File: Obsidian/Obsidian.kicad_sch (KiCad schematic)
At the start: 5 parts

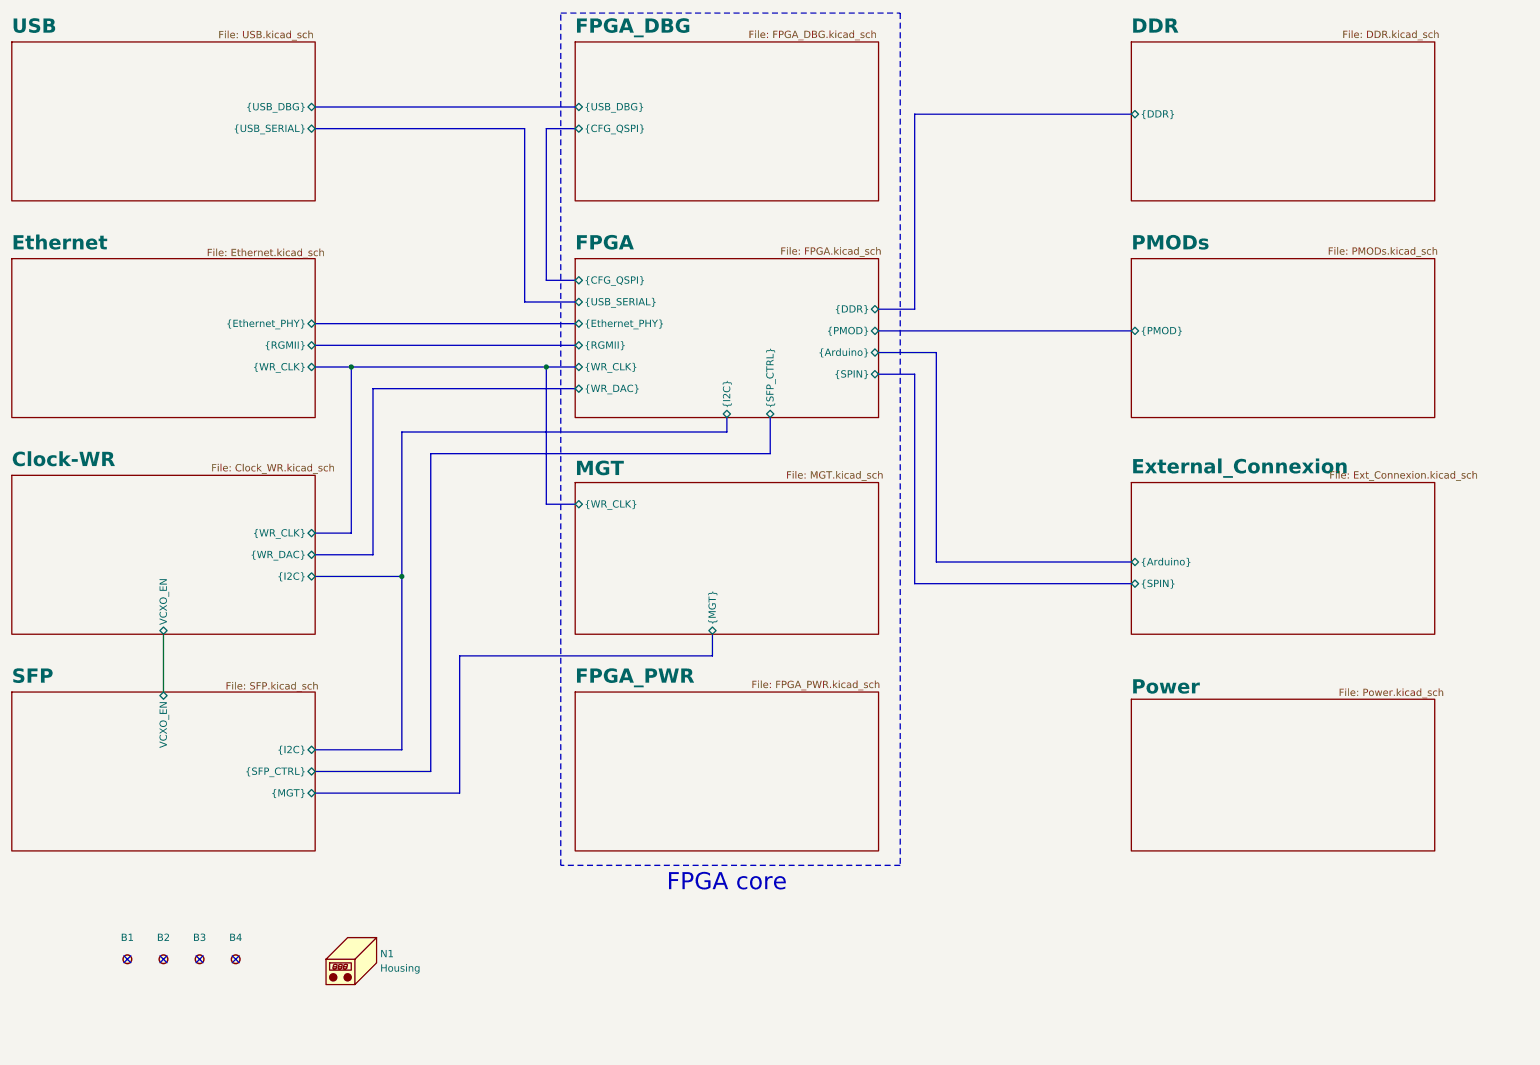
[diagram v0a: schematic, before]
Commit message: removing reset global label
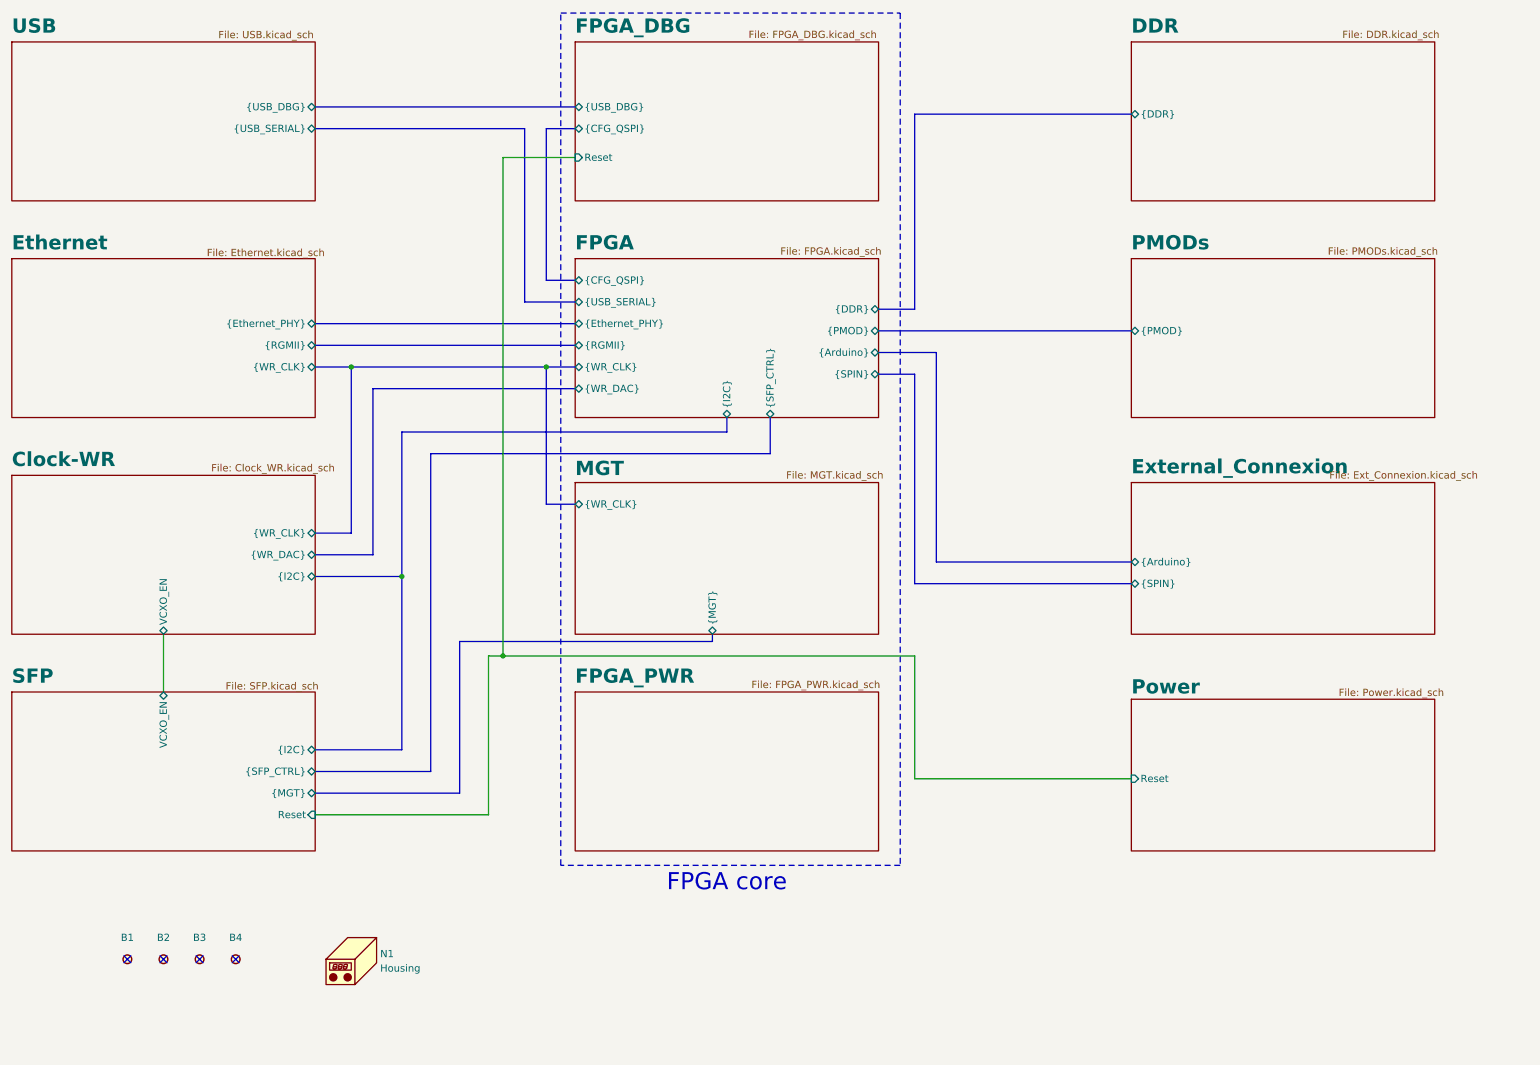
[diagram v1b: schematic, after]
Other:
- sheet FPGA_DBG ports: added Reset; removed none
- sheet Power ports: added Reset; removed none
- sheet SFP ports: added Reset; removed none
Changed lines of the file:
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@@
 	)
 	(junction
+		(at 106.68 127)
+		(diameter 0)
+		(color 0 0 0 0)
+	)
+	(junction
 		(at 88.9 113.03)
 		(diameter 0)
@@
 		)
 	)
+	(wire
+		(pts
+			(xy 104.14 127) (xy 104.14 154.94)
+		)
+		(stroke
+			(width 0)
+			(type default)
+		)
+	)
 	(bus
 		(pts
-			(xy 143.51 127) (xy 99.06 127)
+			(xy 143.51 124.46) (xy 99.06 124.46)
 		)
 		(stroke
@@
 	(bus
 		(pts
-			(xy 99.06 127) (xy 99.06 151.13)
+			(xy 99.06 124.46) (xy 99.06 151.13)
 		)
 		(stroke
@@
 	(bus
 		(pts
-			(xy 143.51 123.19) (xy 143.51 127)
+			(xy 143.51 123.19) (xy 143.51 124.46)
+		)
+		(stroke
+			(width 0)
+			(type default)
+		)
+	)
+	(wire
+		(pts
+			(xy 217.17 148.59) (xy 179.07 148.59)
+		)
+		(stroke
+			(width 0)
+			(type default)
+		)
+	)
+	(wire
+		(pts
+			(xy 179.07 127) (xy 106.68 127)
 		)
 		(stroke
@@
 		)
 	)
+	(wire
+		(pts
+			(xy 104.14 127) (xy 106.68 127)
+		)
+		(stroke
+			(width 0)
+			(type default)
+		)
+	)
+	(wire
+		(pts
+			(xy 119.38 39.37) (xy 106.68 39.37)
+		)
+		(stroke
+			(width 0)
+			(type default)
+		)
+	)
 	(bus
 		(pts
@@
 		)
 	)
+	(wire
+		(pts
+			(xy 179.07 148.59) (xy 179.07 127)
+		)
+		(stroke
+			(width 0)
+			(type default)
+		)
+	)
 	(bus
 		(pts
@@
 		)
 	)
+	(wire
+		(pts
+			(xy 104.14 154.94) (xy 73.66 154.94)
+		)
+		(stroke
+			(width 0)
+			(type default)
+		)
+	)
 	(bus
 		(pts
@@
 		)
 	)
+	(wire
+		(pts
+			(xy 106.68 39.37) (xy 106.68 127)
+		)
+		(stroke
+			(width 0)
+			(type default)
+		)
+	)
 	(bus
 		(pts
@@
 			)
 		)
+		(pin "Reset" input
+			(at 217.17 148.59 180)
+			(effects
+				(font
+					(size 1.27 1.27)
+				)
+				(justify left)
+			)
+		)
 		(instances
 			(project "Obsidian"
@@
 			)
 		)
+		(pin "Reset" input
+			(at 119.38 39.37 180)
+			(effects
+				(font
+					(size 1.27 1.27)
+				)
+				(justify left)
+			)
+		)
 		(instances
 			(project "Obsidian"
@@
 			(effects
 				(font
+					(size 1.27 1.27)
+				)
+				(justify right)
+			)
+		)
+		(pin "Reset" input
+			(at 73.66 154.94 0)
+			(effects
+				(font

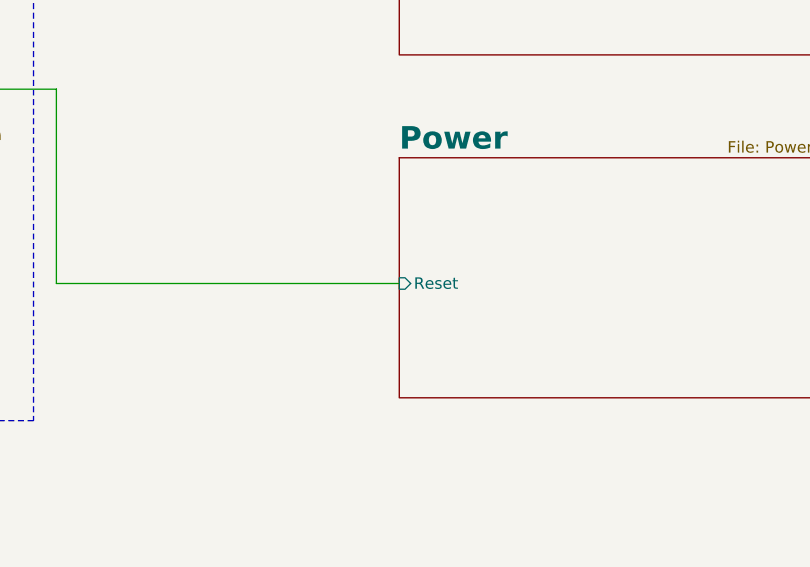
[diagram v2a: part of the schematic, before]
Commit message: Adding documentation for configuration with flash memory, adding more comments to schematic
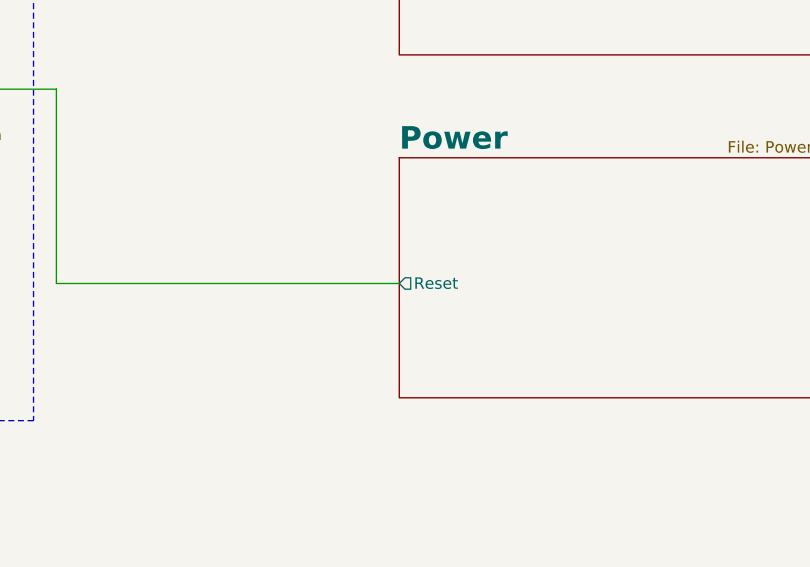
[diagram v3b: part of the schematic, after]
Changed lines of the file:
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@@
 			)
 		)
-		(pin "Reset" input
+		(pin "Reset" output
 			(at 217.17 148.59 180)
 			(effects

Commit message: Cleaning symbol fields
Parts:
- B1, B2, B3, B4: Author CERN DEM JMW -> (none); Case (none) -> (none); Comment (none) -> (none); Component Kind Standard (No BOM) -> (none); Component Type Standard (No BOM) -> (none); ComponentHeight 0mm -> (none); ComponentLink1Description (none) -> (none); ComponentLink1URL (none) -> (none); ComponentLink2Description (none) -> (none); ComponentLink2URL (none) -> (none); CreateDate 10/01/12 00:00:00 -> (none); Database Table Name Eletro-mechanical -> (none); Family Plated Hole -> (none); Footprint Library Pads -> (none); Footprint Path PcbLib\Pads.PcbLib -> (none); Footprint Ref MTG320_550 -> (none); HelpURL Undefined -> (none); LatestRevisionDate 10/01/12 00:00:00 -> (none); Library Name Pads -> (none); Library Path SchLib\Pads.SchLib -> (none); Library Ref Single Terminal Socket -> (none); License CC-BY-SA 4.0 -> (none); Manufacturer (none) -> (none); Manufacturer Part Number (none) -> (none); Manufacturer1 ComponentHeight (none) -> (none); Manufacturer1 Example (none) -> (none); Manufacturer1 Part Number (none) -> (none); Mounted No -> (none); PackageDescription Plated Through Hole: Hole Dia.=3.2mm Pad Dia.=5.5mm -> (none); Part Description Plated Through Hole: Hole Dia.=3.2mm Pad Dia.=5.5mm -> (none); Part Number PLATED_HOLE3.2_PAD5.5 -> (none); Pin Count 1 -> (none); SCEM (none) -> (none); SMD No -> (none); Sense No -> (none); Sense Comment (none) -> (none); Socket No -> (none); Status None -> (none); Status Comment (none) -> (none)

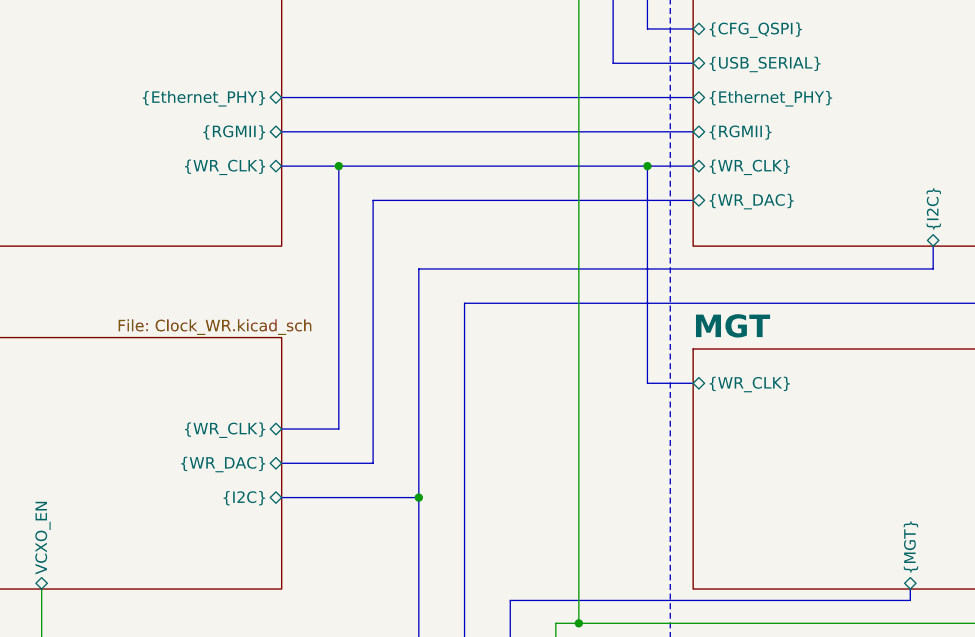
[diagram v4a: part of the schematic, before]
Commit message: Separating auxiliary clock from WR clock
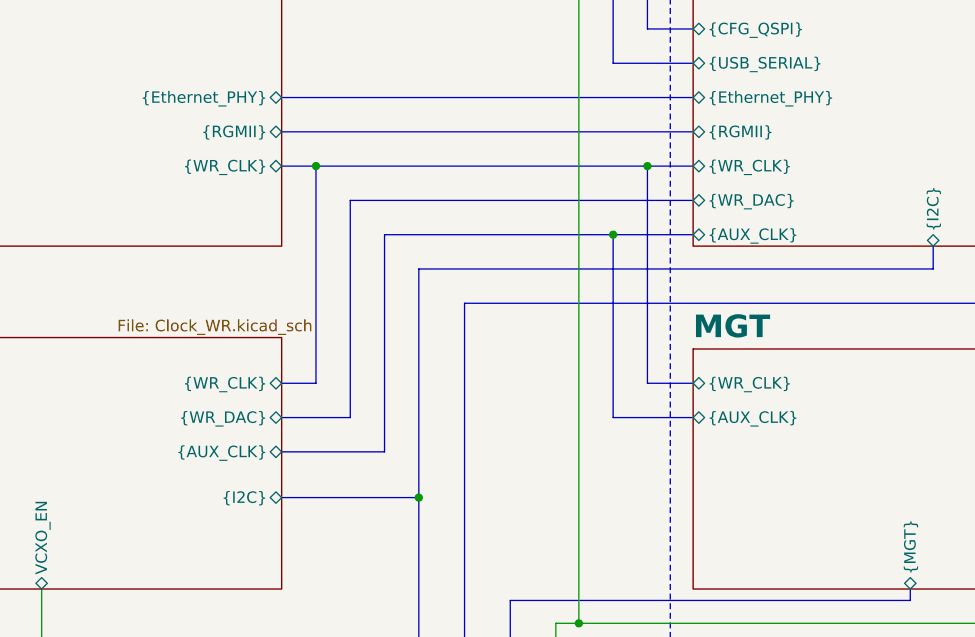
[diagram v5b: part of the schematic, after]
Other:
- sheet Clock-WR ports: added {AUX_CLK}; removed none
- sheet FPGA ports: added {AUX_CLK}; removed none
- sheet MGT ports: added {AUX_CLK}; removed none
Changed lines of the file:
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@@
+	)
+	(junction
+		(at 77.47 76.2)
+		(diameter 0)
+		(color 0 0 0 0)
+	)
+	(junction
+		(at 110.49 83.82)
+		(diameter 0)
+		(color 0 0 0 0)
 	)
 	(junction
@@
 		(color 0 0 0 0)
 	)
-	(junction
-		(at 80.01 76.2)
-		(diameter 0)
-		(color 0 0 0 0)
-	)
 	(no_connect
 		(at 40.64 180.34)
@@
 	(bus
 		(pts
+			(xy 119.38 104.14) (xy 110.49 104.14)
+		)
+		(stroke
+			(width 0)
+			(type default)
+		)
+	)
+	(bus
+		(pts
 			(xy 143.51 124.46) (xy 99.06 124.46)
 		)
@@
 	(bus
 		(pts
-			(xy 80.01 76.2) (xy 80.01 105.41)
-		)
-		(stroke
-			(width 0)
-			(type default)
-		)
-	)
-	(bus
-		(pts
-			(xy 73.66 76.2) (xy 80.01 76.2)
+			(xy 77.47 76.2) (xy 77.47 100.33)
+		)
+		(stroke
+			(width 0)
+			(type default)
+		)
+	)
+	(bus
+		(pts
+			(xy 73.66 76.2) (xy 77.47 76.2)
 		)
 		(stroke
@@
 	(bus
 		(pts
+			(xy 73.66 107.95) (xy 85.09 107.95)
+		)
+		(stroke
+			(width 0)
+			(type default)
+		)
+	)
+	(bus
+		(pts
 			(xy 182.88 110.49) (xy 217.17 110.49)
 		)
@@
 	(bus
 		(pts
+			(xy 110.49 104.14) (xy 110.49 83.82)
+		)
+		(stroke
+			(width 0)
+			(type default)
+		)
+	)
+	(bus
+		(pts
 			(xy 93.98 147.32) (xy 73.66 147.32)
 		)
@@
 	(bus
 		(pts
+			(xy 110.49 83.82) (xy 119.38 83.82)
+		)
+		(stroke
+			(width 0)
+			(type default)
+		)
+	)
+	(bus
+		(pts
 			(xy 114.3 34.29) (xy 114.3 60.96)
 		)
@@
 	(bus
 		(pts
+			(xy 77.47 76.2) (xy 114.3 76.2)
+		)
+		(stroke
+			(width 0)
+			(type default)
+		)
+	)
+	(bus
+		(pts
 			(xy 73.66 72.39) (xy 119.38 72.39)
 		)
@@
 	(bus
 		(pts
-			(xy 80.01 76.2) (xy 114.3 76.2)
-		)
-		(stroke
-			(width 0)
-			(type default)
-		)
-	)
-	(bus
-		(pts
 			(xy 73.66 34.29) (xy 110.49 34.29)
 		)
@@
 	(bus
 		(pts
-			(xy 119.38 80.01) (xy 83.82 80.01)
+			(xy 119.38 80.01) (xy 81.28 80.01)
 		)
 		(stroke
@@
 	(bus
 		(pts
-			(xy 73.66 105.41) (xy 80.01 105.41)
+			(xy 73.66 100.33) (xy 77.47 100.33)
 		)
 		(stroke
@@
 	(bus
 		(pts
-			(xy 83.82 80.01) (xy 83.82 109.22)
+			(xy 81.28 80.01) (xy 81.28 104.14)
 		)
 		(stroke
@@
 	(bus
 		(pts
+			(xy 85.09 107.95) (xy 85.09 83.82)
+		)
+		(stroke
+			(width 0)
+			(type default)
+		)
+	)
+	(bus
+		(pts
+			(xy 85.09 83.82) (xy 110.49 83.82)
+		)
+		(stroke
+			(width 0)
+			(type default)
+		)
+	)
+	(bus
+		(pts
 			(xy 93.98 91.44) (xy 93.98 147.32)
 		)
@@
 	(bus
 		(pts
-			(xy 83.82 109.22) (xy 73.66 109.22)
+			(xy 81.28 104.14) (xy 73.66 104.14)
 		)
 		(stroke
@@
 			)
 		)
+		(pin "{AUX_CLK}" bidirectional
+			(at 119.38 83.82 180)
+			(effects
+				(font
+					(size 1.27 1.27)
+				)
+				(justify left)
+			)
+		)
 		(instances
 			(project "Obsidian"
@@
 			)
 		)
+		(pin "{AUX_CLK}" bidirectional
+			(at 119.38 104.14 180)
+			(effects
+				(font
+					(size 1.27 1.27)
+				)
+				(justify left)
+			)
+		)
 		(instances
 			(project "Obsidian"
@@
 		)
 		(pin "{WR_CLK}" bidirectional
-			(at 73.66 105.41 0)
+			(at 73.66 100.33 0)
 			(effects
 				(font
@@
 		)
 		(pin "{WR_DAC}" bidirectional
-			(at 73.66 109.22 0)
+			(at 73.66 104.14 0)
 			(effects
 				(font
@@
 			)
 		)
+		(pin "{AUX_CLK}" bidirectional
+			(at 73.66 107.95 0)
+			(effects
+				(font
+					(size 1.27 1.27)
+				)
+				(justify right)
+			)
+		)

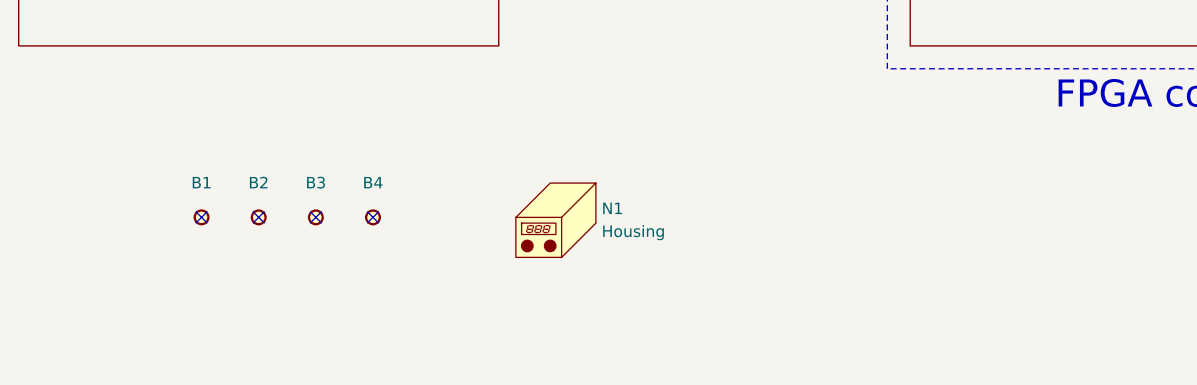
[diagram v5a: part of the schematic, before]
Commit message: Adding the gnd shield
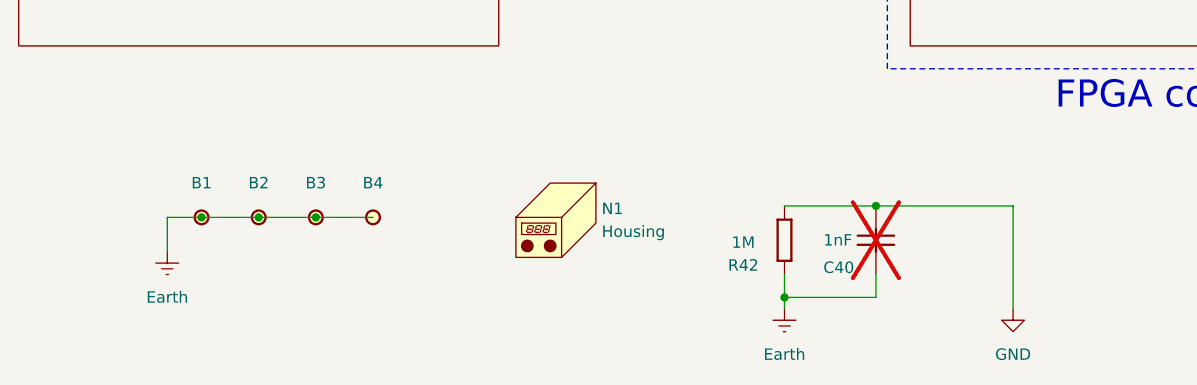
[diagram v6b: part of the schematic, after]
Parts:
- added C40: CC0201_1NF_25V_5%_C0G, Footprint:CAPC0603X33N, symbol Library_Symbol:CC0201_100NF_6.3V_10%_X5R
- added R42: R0402_1MR_1%_0.0625W_100PPM, Footprint:RESC1005X40N, symbol Library_Symbol:R0402_240R_1%_0.0625W_100PPM
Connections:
- net Earth: now reaches B4.1
- net Earth: now also B1.1, B2.1, B3.1, C40.2, R42.2
- new net GND: C40.1, R42.1
- no-connect marks 4 -> 0
